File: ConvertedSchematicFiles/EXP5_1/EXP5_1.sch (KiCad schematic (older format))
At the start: 8 parts

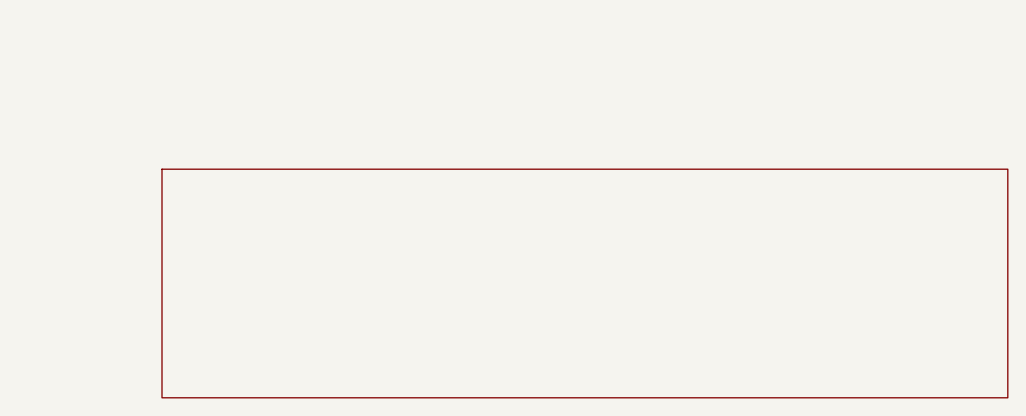
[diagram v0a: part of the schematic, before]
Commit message: Excluded some components. These no longer appear after conversion. When calling shell commands, filenames are in "quotes"
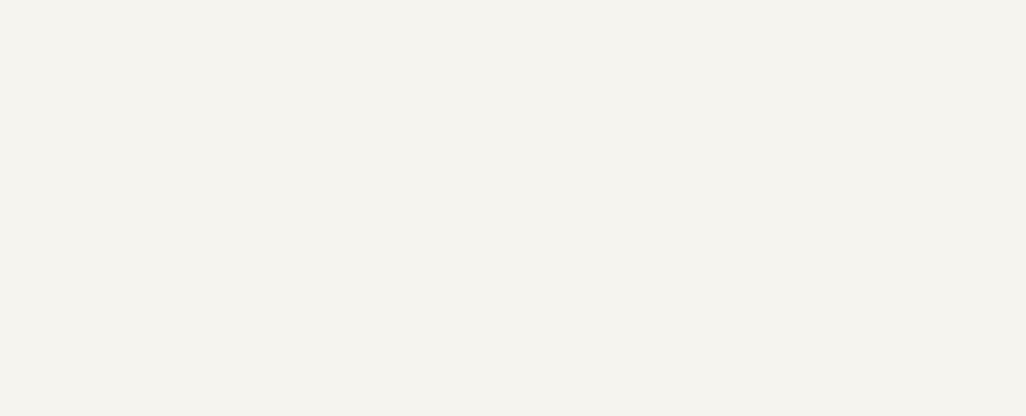
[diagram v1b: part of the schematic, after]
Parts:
- removed titleblk: titleblk, symbol TITLEBLK_PSPICE
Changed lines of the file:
@@
 	0    -1    1    0
-$EndComp
-$Comp
-L TITLEBLK_PSPICE titleblk
-U 1 1 39760492
-P 9700 7200
-F 0 "titleblk" H 19400 14400 30  0001 L CNN
-F 1 "titleblk" H 19400 14480 30  0001 L CNN
-	1    9700 7200
-	1    0    0    1
 $EndComp
 Wire Wire Line

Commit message: Ports issue fixed. Now annotation for ports is #PWR? function added "itos"
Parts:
- removed EGND: EGND, symbol EGND_PSPICE
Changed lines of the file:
@@
 $EndDescr
 $Comp
-L EGND_PSPICE EGND
+L EGND_PSPICE #PWR1
 U 1 1 14289383
 P 2800 1700
-F 0 "EGND" H 5600 3400 30  0001 L CNN
+F 0 "#PWR1" H 5600 3400 30  0001 L CNN
 F 1 "EGND" H 5600 3480 30  0001 L CNN
 	1    2800 1700

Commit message: Added LICENSE.txt
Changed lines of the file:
@@
 $EndDescr
 $Comp
-L EGND_PSPICE #PWR1
+L GND #PWR1
 U 1 1 14289383
 P 2800 1700

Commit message: Orientation fix. Library components are now inverted, with +ve y axis going up. In Schematic files, +ve y axis is downwards. This is how the KiCad libraries are. As a result of the above fixed, the converted GND is now oriented correctly.
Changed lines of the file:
@@
 F 1 "EGND" H 5600 3480 30  0001 L CNN
 	1    2800 1700
-	1    0    0    1
+	1    0    0    -1
 $EndComp
 $Comp
@@
 F 1 "10A" H 1100 1810 30  0000 C CNN
 	1    1100 1500
-	-1    0    0    -1
+	-1    0    0    1
 $EndComp
 $Comp
@@
 F 1 "INCLUDE" H 3100 2080 30  0001 L CNN
 	1    3100 2000
-	1    0    0    1
+	1    0    0    -1
 $EndComp
 $Comp
@@
 F 1 "5A" H 2800 1410 30  0000 C CNN
 	1    2800 1500
-	-1    0    0    -1
+	-1    0    0    1
 $EndComp
 $Comp
@@
 F 1 "15A" H 2200 1410 30  0000 C CNN
 	1    2200 1500
-	-1    0    0    -1
+	-1    0    0    1
 $EndComp
 $Comp
@@
 F 1 "20A" H 1700 960 30  0000 C CNN
 	1    1700 1100
-	1    0    0    1
+	1    0    0    -1
 $EndComp
 $Comp
@@
 F 1 "2" H 3400 1500 30  0000 L CNN
 	1    3400 1200
-	0    -1    1    0
+	0    1    1    0
 $EndComp
 Wire Wire Line

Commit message: Removed the use of exec, wrote basename function, made integration with eSim easier.
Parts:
- added titleblk: titleblk, symbol titleblk_PSPICE
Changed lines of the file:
@@
-EESchema Schematic File Version 2  date Friday 25 February 2000 06:44:10 PM IST
+EESchema Schematic File Version 2  date
 LIBS:power
 LIBS:device
@@
 LIBS:contrib
 LIBS:valves
-LIBS:ConvertedSchematicFiles/EXP5_1-cache
 EELAYER 25  0
 EELAYER END
@@
 Sheet 1 1
 Title ""
-Date "25 Feb 2000"
+Date ""
 Rev ""
 Comp ""
@@
 	0    1    1    0
 $EndComp
+$Comp
+L titleblk_PSPICE titleblk
+U 1 1 39760492
+P 9700 7200
+F 0 "titleblk" H 19400 14400 30  0001 L CNN
+F 1 "titleblk" H 19400 14480 30  0001 L CNN
+	1    9700 7200
+	1    0    0    -1
+$EndComp
 Wire Wire Line
